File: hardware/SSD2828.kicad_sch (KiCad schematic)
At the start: 64 parts, among them IC1 TLV62568DBVR, J1 FH35C-25S-0.3SHW_50_, J3 Conn_01x34, U1 PAM2306DYPAA, U2 SSD2828QN4, Y1 24mhz

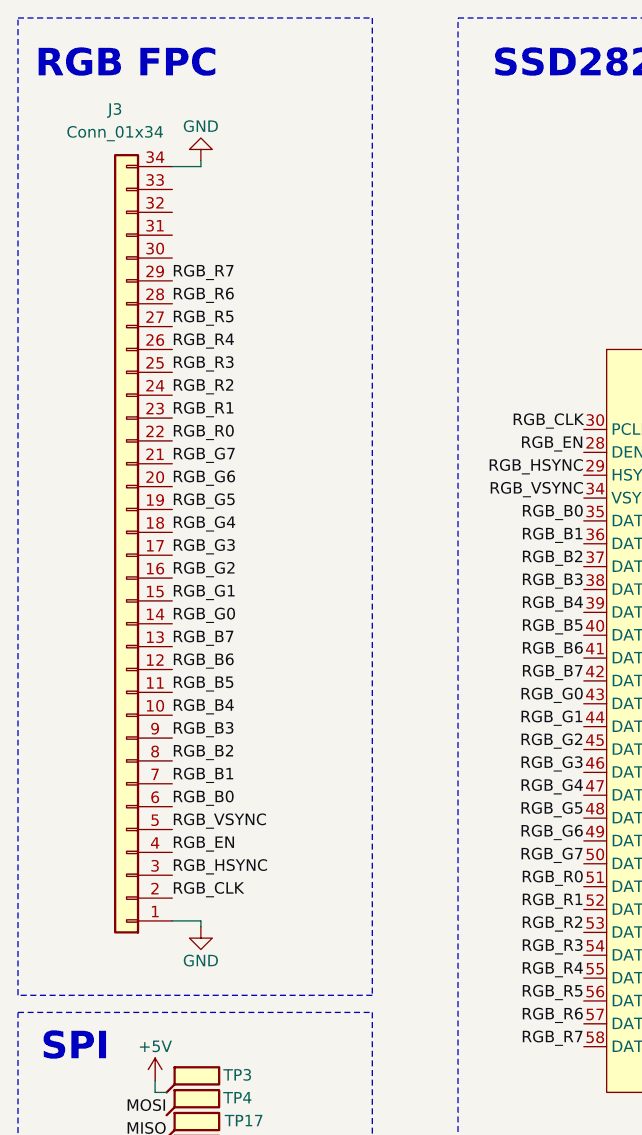
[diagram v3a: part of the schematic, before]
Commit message: routed 1v2 to ssd2828 + finished debug board
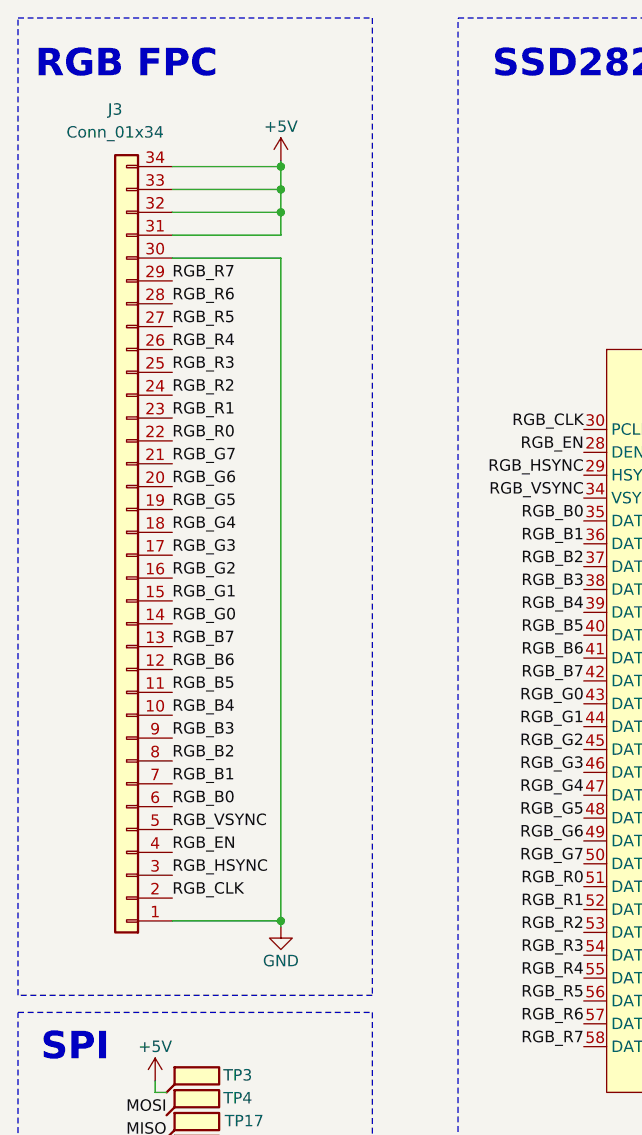
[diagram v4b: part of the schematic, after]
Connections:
- net +5V: now also J3.31 (Pin_31), J3.32 (Pin_32), J3.33 (Pin_33), J3.34 (Pin_34)
- net GND: now also J3.30 (Pin_30); no longer J3.34 (Pin_34)
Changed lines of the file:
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@@
   (junction (at 132.08 137.16) (diameter 0) (color 0 0 0 0)
   )
+  (junction (at 43.815 31.115) (diameter 0) (color 0 0 0 0)
+  )
   (junction (at 196.85 36.83) (diameter 0) (color 0 0 0 0)
   )
@@
   (junction (at 248.285 35.56) (diameter 0) (color 0 0 0 0)
   )
+  (junction (at 43.815 114.935) (diameter 0) (color 0 0 0 0)
+  )
   (junction (at 264.16 20.955) (diameter 0) (color 0 0 0 0)
   )
@@
   (junction (at 127 137.16) (diameter 0) (color 0 0 0 0)
   )
+  (junction (at 43.815 36.195) (diameter 0) (color 0 0 0 0)
+  )
   (junction (at 127 31.75) (diameter 0) (color 0 0 0 0)
   )
@@
   (junction (at 118.11 48.26) (diameter 0) (color 0 0 0 0)
   )
+  (junction (at 43.815 33.655) (diameter 0) (color 0 0 0 0)
+  )
   (junction (at 127 26.035) (diameter 0) (color 0 0 0 0)
   )
@@
     (stroke (width 0) (type default))
   )
+  (wire (pts (xy 31.75 36.195) (xy 43.815 36.195))
+    (stroke (width 0) (type default))
+  )
   (wire (pts (xy 264.795 41.91) (xy 264.795 43.18))
     (stroke (width 0) (type default))
@@
     (stroke (width 0) (type default))
   )
-  (wire (pts (xy 34.925 114.935) (xy 34.925 115.57))
+  (wire (pts (xy 43.815 114.935) (xy 43.815 115.57))
     (stroke (width 0) (type default))
   )
@@
     (stroke (width 0) (type default))
   )
-  (wire (pts (xy 34.925 31.115) (xy 34.925 30.48))
-    (stroke (width 0) (type default))
-  )
   (wire (pts (xy 133.35 48.26) (xy 133.35 48.895))
     (stroke (width 0) (type default))
@@
     (stroke (width 0) (type default))
   )
-  (wire (pts (xy 31.75 114.935) (xy 34.925 114.935))
+  (wire (pts (xy 31.75 114.935) (xy 43.815 114.935))
     (stroke (width 0) (type default))
   )
@@
     (stroke (width 0) (type default))
   )
+  (wire (pts (xy 31.75 38.735) (xy 43.815 38.735))
+    (stroke (width 0) (type default))
+  )
+  (wire (pts (xy 43.815 31.115) (xy 43.815 30.48))
+    (stroke (width 0) (type default))
+  )
   (wire (pts (xy 29.845 132.715) (xy 29.845 133.985))
     (stroke (width 0) (type default))
@@
     (stroke (width 0) (type default))
   )
+  (wire (pts (xy 43.815 38.735) (xy 43.815 36.195))
+    (stroke (width 0) (type default))
+  )
   (wire (pts (xy 247.65 81.915) (xy 255.27 81.915))
     (stroke (width 0) (type default))
@@
     (stroke (width 0) (type default))
   )
+  (wire (pts (xy 43.815 33.655) (xy 43.815 31.115))
+    (stroke (width 0) (type default))
+  )
   (wire (pts (xy 38.735 175.895) (xy 41.275 175.895))
     (stroke (width 0) (type default))
@@
     (stroke (width 0) (type default))
   )
+  (wire (pts (xy 31.75 31.115) (xy 43.815 31.115))
+    (stroke (width 0) (type default))
+  )
   (wire (pts (xy 28.575 175.895) (xy 31.115 175.895))
     (stroke (width 0) (type default))
@@
     (stroke (width 0) (type default))
   )
+  (wire (pts (xy 43.815 41.275) (xy 43.815 114.935))
+    (stroke (width 0) (type default))
+  )
   (wire (pts (xy 247.65 129.54) (xy 261.62 129.54))
     (stroke (width 0) (type default))
@@
     (stroke (width 0) (type default))
   )
+  (wire (pts (xy 31.75 33.655) (xy 43.815 33.655))
+    (stroke (width 0) (type default))
+  )
   (wire (pts (xy 238.125 40.64) (xy 240.665 40.64))
     (stroke (width 0) (type default))
@@
     (stroke (width 0) (type default))
   )
+  (wire (pts (xy 31.75 41.275) (xy 43.815 41.275))
+    (stroke (width 0) (type default))
+  )
   (wire (pts (xy 97.155 34.925) (xy 102.235 34.925))
     (stroke (width 0) (type default))
@@
     (stroke (width 0) (type default))
   )
+  (wire (pts (xy 43.815 36.195) (xy 43.815 33.655))
+    (stroke (width 0) (type default))
+  )
   (wire (pts (xy 127 20.955) (xy 118.745 20.955))
     (stroke (width 0) (type default))
@@
   )
   (wire (pts (xy 247.65 144.78) (xy 252.73 144.78))
-    (stroke (width 0) (type default))
-  )
-  (wire (pts (xy 31.75 31.115) (xy 34.925 31.115))
     (stroke (width 0) (type default))
   )
@@
     )
   )
+  (symbol (lib_name "+5V_1") (lib_id "power:+5V") (at 43.815 30.48 0) (unit 1)
+    (in_bom yes) (on_board yes) (dnp no) (fields_autoplaced)
+    (property "Reference" "#PWR04" (at 43.815 34.29 0)
+      (effects (font (size 1.27 1.27)) hide)
+    )
+    (property "Value" "+5V" (at 43.815 26.67 0)
+      (effects (font (size 1.27 1.27)))
+    )
+    (property "Footprint" "" (at 43.815 30.48 0)
+      (effects (font (size 1.27 1.27)) hide)
+    )
+    (property "Datasheet" "" (at 43.815 30.48 0)
+      (effects (font (size 1.27 1.27)) hide)
+    )
+    (pin "1")
+    (instances
+      (project "ssd2828_board"
+        (path "/e63e39d7-6ac0-4ffd-8aa3-1841a4541b55"
+          (reference "#PWR04") (unit 1)
+        )
+        (path "/e63e39d7-6ac0-4ffd-8aa3-1841a4541b55/eadf4466-e824-4ab1-a46a-9025d68137a1"
+          (reference "#PWR098") (unit 1)
+        )
+      )
+    )
+  )
   (symbol (lib_id "Device:C_Small") (at 151.765 23.495 0) (mirror y) (unit 1)
     (in_bom yes) (on_board yes) (dnp no)
@@
     )
   )
-  (symbol (lib_name "GND_1") (lib_id "power:GND") (at 34.925 115.57 0) (unit 1)
-    (in_bom yes) (on_board yes) (dnp no)
-    (property "Reference" "#PWR014" (at 34.925 121.92 0)
-      (effects (font (size 1.27 1.27)) hide)
-    )
-    (property "Value" "GND" (at 34.925 119.38 0)
-      (effects (font (size 1.27 1.27)))
-    )
-    (property "Footprint" "" (at 34.925 115.57 0)
-      (effects (font (size 1.27 1.27)) hide)
-    )
-    (property "Datasheet" "" (at 34.925 115.57 0)
+  (symbol (lib_name "GND_1") (lib_id "power:GND") (at 43.815 115.57 0) (unit 1)
+    (in_bom yes) (on_board yes) (dnp no)
+    (property "Reference" "#PWR014" (at 43.815 121.92 0)
+      (effects (font (size 1.27 1.27)) hide)
+    )
+    (property "Value" "GND" (at 43.815 119.38 0)
+      (effects (font (size 1.27 1.27)))
+    )
+    (property "Footprint" "" (at 43.815 115.57 0)
+      (effects (font (size 1.27 1.27)) hide)
+    )
+    (property "Datasheet" "" (at 43.815 115.57 0)
       (effects (font (size 1.27 1.27)) hide)
     )
@@
         )
       )
-    )
-  )
-  (symbol (lib_name "GND_3") (lib_id "power:GND") (at 34.925 30.48 180) (unit 1)
-    (in_bom yes) (on_board yes) (dnp no) (fields_autoplaced)
-    (property "Reference" "#PWR03" (at 34.925 24.13 0)
-      (effects (font (size 1.27 1.27)) hide)
-    )
-    (property "Value" "GND" (at 34.925 26.67 0)
-      (effects (font (size 1.27 1.27)))
-    )
-    (property "Footprint" "" (at 34.925 30.48 0)
-      (effects (font (size 1.27 1.27)) hide)
-    )
-    (property "Datasheet" "" (at 34.925 30.48 0)
-      (effects (font (size 1.27 1.27)) hide)
-    )
-    (pin "1")
-    (instances
-      (project "ssd2828_board"
-        (path "/e63e39d7-6ac0-4ffd-8aa3-1841a4541b55"
-          (reference "#PWR03") (unit 1)
-        )
-        (path "/e63e39d7-6ac0-4ffd-8aa3-1841a4541b55/eadf4466-e824-4ab1-a46a-9025d68137a1"
-          (reference "#PWR021") (unit 1)
-        )
-      )

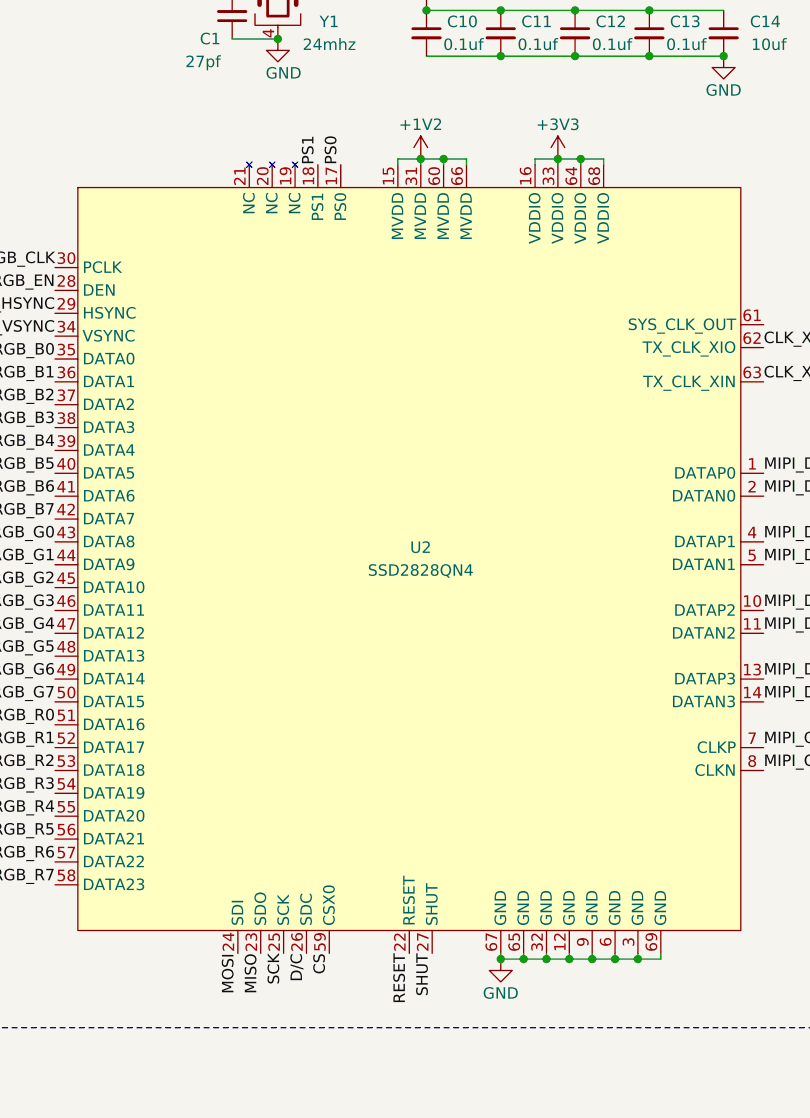
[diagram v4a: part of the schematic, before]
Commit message: making the project portableby moving external libaries to the project
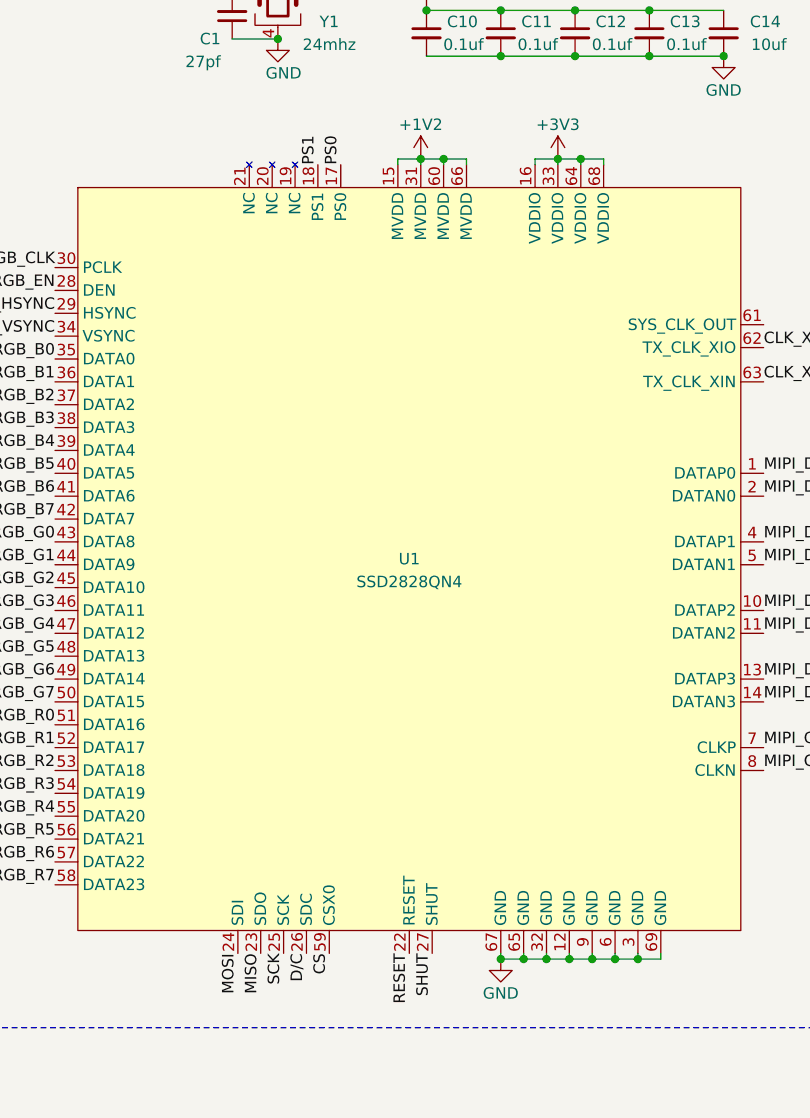
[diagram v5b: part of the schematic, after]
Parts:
- removed U2: SSD2828QN4, Package_DFN_QFN:QFN-68-1EP_8x8mm_P0.4mm_EP5.2x5.2mm, symbol Video:SSD2828QN4
- added U1: SSD2828QN4, Package_DFN_QFN:QFN-68-1EP_8x8mm_P0.4mm_EP5.2x5.2mm, symbol ssd2828:SSD2828QN4
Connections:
- net +1V2: now also U1.15 (MVDD), U1.31 (MVDD), U1.60 (MVDD), U1.66 (MVDD)
- net +3V3: now also U1.16 (VDDIO), U1.33 (VDDIO), U1.64 (VDDIO), U1.68 (VDDIO)
- net CLK_XIN: now also U1.63 (TX_CLK_XIN)
- net CLK_XIO: now also U1.62 (TX_CLK_XIO)
- net CS: now also U1.59 (CSX0)
- net D/C: now also U1.26 (SDC)
- net GND: now also U1.12 (GND), U1.3 (GND), U1.32 (GND), U1.6 (GND), U1.65 (GND), U1.67 (GND), U1.69 (GND), U1.9 (GND)
- net MIPI_CLK_N: now also U1.8 (CLKN)
- net MIPI_CLK_P: now also U1.7 (CLKP)
- net MIPI_DATA0_N: now also U1.2 (DATAN0)
- net MIPI_DATA0_P: now also U1.1 (DATAP0)
- net MIPI_DATA1_N: now also U1.5 (DATAN1)
- net MIPI_DATA1_P: now also U1.4 (DATAP1)
- net MIPI_DATA2_N: now also U1.11 (DATAN2)
- net MIPI_DATA2_P: now also U1.10 (DATAP2)
- net MIPI_DATA3_N: now also U1.14 (DATAN3)
- net MIPI_DATA3_P: now also U1.13 (DATAP3)
- net MISO: now also U1.23 (SDO)
- net MOSI: now also U1.24 (SDI)
- net PS0: now also U1.17 (PS0)
- net PS1: now also U1.18 (PS1)
- net RESET: now also U1.22 (RESET)
- net RGB_B0: now also U1.35 (DATA0)
- net RGB_B1: now also U1.36 (DATA1)
- net RGB_B2: now also U1.37 (DATA2)
- net RGB_B3: now also U1.38 (DATA3)
- net RGB_B4: now also U1.39 (DATA4)
- net RGB_B5: now also U1.40 (DATA5)
- net RGB_B6: now also U1.41 (DATA6)
- net RGB_B7: now also U1.42 (DATA7)
- net RGB_CLK: now also U1.30 (PCLK)
- net RGB_EN: now also U1.28 (DEN)
- net RGB_G0: now also U1.43 (DATA8)
- net RGB_G1: now also U1.44 (DATA9)
- net RGB_G2: now also U1.45 (DATA10)
- net RGB_G3: now also U1.46 (DATA11)
- net RGB_G4: now also U1.47 (DATA12)
- net RGB_G5: now also U1.48 (DATA13)
- net RGB_G6: now also U1.49 (DATA14)
- net RGB_G7: now also U1.50 (DATA15)
- net RGB_HSYNC: now also U1.29 (HSYNC)
- net RGB_R0: now also U1.51 (DATA16)
- net RGB_R1: now also U1.52 (DATA17)
- net RGB_R2: now also U1.53 (DATA18)
- net RGB_R3: now also U1.54 (DATA19)
- net RGB_R4: now also U1.55 (DATA20)
- net RGB_R5: now also U1.56 (DATA21)
- net RGB_R6: now also U1.57 (DATA22)
- net RGB_R7: now also U1.58 (DATA23)
- net RGB_VSYNC: now also U1.34 (VSYNC)
- net SCK: now also U1.25 (SCK)
- net SHUT: now also U1.27 (SHUT)
